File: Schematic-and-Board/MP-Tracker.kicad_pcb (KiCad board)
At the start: 2 copper layers, 61 parts, among them P1 DIL10, Q1 BC817, Q2 IRFR5303, Q3 BC817-40, Q4 IRFR5303, U1 MC34063, U2 TL082, U3 ATMEGA8-AI, U4 MC78L033, X1 3.6864MHz

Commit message: Update schematic and board design and firmware source.
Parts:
- removed D3, D6: 3V3, Diodes_SMD:SOD-123
- removed R17: 1k, Resistors_SMD:R_0805
- removed R18, R23, R24, R28, R29: 22k, Resistors_SMD:R_0805
- added ?: , Mounting_Holes:MountingHole_3.2mm_M3_DIN965, F.Cu at (167.6, 70.5)
- added ?: , Mounting_Holes:MountingHole_3.2mm_M3_DIN965, F.Cu at (99.9, 141.5)
- added C14: 330u, Capacitors_SMD:c_elec_10x10, F.Cu at (151.7, 132.0)
- added C16: 470n, Capacitors_SMD:C_1206_HandSoldering, F.Cu at (150.3, 77.4)
- added C17: 470n, Capacitors_SMD:C_1206_HandSoldering, F.Cu at (123.2, 95.3)
- added C18: 470n, Capacitors_SMD:C_1206_HandSoldering, F.Cu at (127.3, 90.3)
- added D7: 1N4001, Diodes_SMD:SOD-323, F.Cu at (99.3, 134.5)
- added D9: 1N4001, Diodes_SMD:SOD-323, F.Cu at (159.3, 132.6)
- added L2: 10u, Choke_SMD:Choke_SMD_12x12mm_h8mm, F.Cu at (144.3, 116.8)
- added P2: CON_2x1, Pin_Headers:Pin_Header_Straight_1x02, F.Cu at (145.3, 70.3)
- added R11: 22k, Resistors_SMD:R_0805, F.Cu at (144.9, 90.0)
- added R31: 1K, Resistors_SMD:R_0805, F.Cu at (121.2, 91.8)
- added R32: 1K, Resistors_SMD:R_0805, F.Cu at (125.2, 92.7)
- added REF**: , Mounting_Holes:MountingHole_3.2mm_M3_DIN965, F.Cu at (100.6, 70.1)
- added REF**: , Mounting_Holes:MountingHole_3.2mm_M3_DIN965, F.Cu at (167.6, 141.2)
- C1, C10, C2, C3, C7: value 100n -> 470n; footprint Capacitors_SMD:C_0805 -> Capacitors_SMD:C_1206
- C12: value 10n -> 470n; footprint Capacitors_SMD:C_0805 -> Capacitors_SMD:C_1206
- C8: value 1n5 -> 68p
- L1: value 22u -> 100u
- P1: value DIL10 -> (none)
- Q1: value BC817 -> BC817-40
- R1: value 180R -> 1k
- R12: value 3k9 -> 3k3
- R13: value 3K9 -> 10k
- R15: footprint Resistors_SMD:R_0805 -> Resistors_SMD:R_1206
- R19: value 3k9 -> 10k
- R20: value 47k -> 27k
- R21: value 4k4 -> 2k35
- R22: value 1M -> 47
- R25: value 2k2 -> 1K
- U2: value TL082 -> TL081
- U3: value ATMEGA8-AI -> ATMEGA8
- moved R25 30.5 mm to (124.4, 69.7)
- moved R10 19.0 mm to (134.9, 91.0), turned to 0 degrees
- moved R26 15.6 mm to (139.1, 76.5)
- moved R5 14.0 mm to (154.8, 103.6)
- moved D2 11.9 mm to (166.5, 132.6), turned to 270 degrees
- moved C9 11.7 mm to (101.7, 134.9)
- moved D1 11.4 mm to (104.0, 114.8), turned to 0 degrees
- moved C6 11.3 mm to (109.0, 131.4)
- moved R15 11.3 mm to (139.4, 93.9)
- moved R19 11.3 mm to (144.0, 86.1)
- moved R2 11.3 mm to (103.4, 109.5)
- moved R4 11.3 mm to (155.8, 111.6)
- moved R8 11.3 mm to (125.5, 75.9)
- moved C5 11.3 mm to (103.2, 94.0)
- moved C1 11.3 mm to (133.5, 86.0)
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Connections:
- D1 pad 1: Net-(D1-Pad1) -> Net-(D1-Pad2)
- D1 pad 2: Net-(D1-Pad2) -> Net-(D1-Pad1)
- D2 pad 1: GNDPWR -> VAA
- D2 pad 2: VAA -> GNDPWR
- P1 pad 10: +3.3V -> GNDPWR
- P1 pad 4: Net-(P1-Pad4) -> +3.3V
- P1 pad 7: GNDPWR -> Net-(P1-Pad7)
- R10 pad 1: Net-(R10-Pad1) -> Net-(C18-Pad1)
- R22 pad 1: Net-(R18-Pad2) -> VCC
- R22 pad 2: GNDPWR -> Net-(C16-Pad1)
- R25 pad 1: Net-(R18-Pad2) -> Net-(R25-Pad1)
- U2 pad 1: Net-(R19-Pad1) -> (no net)
- U2 pad 5: Net-(R23-Pad2) -> (no net)
- U2 pad 6: Net-(R18-Pad2) -> Net-(R19-Pad1)
- U2 pad 7: Net-(R17-Pad2) -> Net-(C16-Pad1)
- U2 pad 8: VCC -> (no net)
- U3 pad 1: Net-(U3-Pad1) -> (no net)
- U3 pad 10: Net-(U3-Pad10) -> (no net)
- U3 pad 12: Net-(U3-Pad12) -> (no net)
- U3 pad 13: Net-(R10-Pad1) -> Net-(R31-Pad1)
- U3 pad 14: Net-(U3-Pad14) -> (no net)
- U3 pad 16: Net-(P1-Pad5) -> Net-(P1-Pad2)
- U3 pad 17: Net-(P1-Pad4) -> Net-(P1-Pad3)
- U3 pad 19: Net-(U3-Pad19) -> (no net)
- U3 pad 2: Net-(U3-Pad2) -> (no net)
- U3 pad 22: Net-(U3-Pad22) -> (no net)
- U3 pad 24: Net-(D3-Pad1) -> (no net)
- U3 pad 26: Net-(U3-Pad26) -> Net-(R25-Pad1)
- U3 pad 27: Net-(U3-Pad27) -> (no net)
- U3 pad 28: Net-(U3-Pad28) -> (no net)
- U3 pad 29: Net-(P1-Pad3) -> Net-(P1-Pad9)
- U3 pad 30: Net-(P1-Pad9) -> Net-(P1-Pad7)
- U3 pad 31: Net-(P1-Pad2) -> Net-(P1-Pad5)
- U3 pad 32: Net-(U3-Pad32) -> (no net)
- U3 pad 9: Net-(U3-Pad9) -> (no net)
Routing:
- net GNDPWR: track 471.2 -> 756.0 mm, vias 16 -> 25
- net VCC: track 180.8 -> 282.0 mm
- net Net-(Q3-Pad1): track 169.8 -> 259.6 mm
- net Net-(P1-Pad2): track 13.5 -> 99.0 mm
- net Net-(P1-Pad4): track 84.9 -> 0.00 mm
- net Net-(P1-Pad5): track 74.4 -> 11.1 mm
- net Net-(P1-Pad1): track 54.3 -> 92.9 mm
- net +3.3V: track 59.7 -> 93.0 mm
- net +BATT: track 121.4 -> 147.9 mm
- net Net-(R19-Pad2): track 32.3 -> 51.6 mm
- net Net-(R17-Pad2): track 18.5 -> 0.00 mm
- net Net-(Q3-Pad3): track 42.3 -> 23.9 mm
- net Net-(P1-Pad3): track 19.6 -> 36.4 mm
- net Net-(C18-Pad1): track 0.00 -> 16.0 mm
- net Net-(R18-Pad2): track 15.7 -> 0.00 mm
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- added copper zone on B.Cu, net GNDPWR
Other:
- net class Small added: clearance 0.2, trace_width 0.2, via_dia 1, via_drill 0.8
- board text added: "3V3"
- board text added: "GND"
- board text added: "MISO"
- board text added: "MOSI"
- board text added: "RST"
- board text added: "RX"
- board text added: "SCL"
- board text added: "TX"

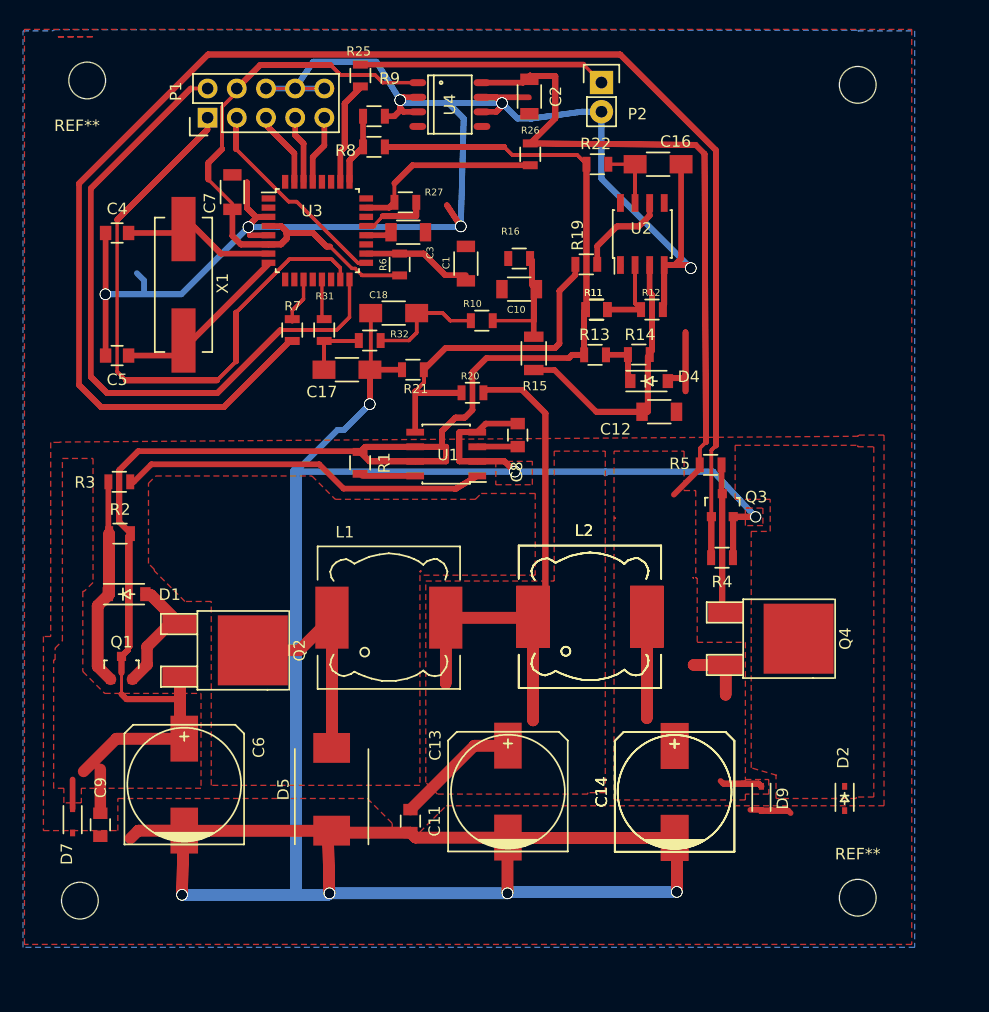
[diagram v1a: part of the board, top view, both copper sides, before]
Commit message: Updated firmware with temperature sensor support (KTY81-210) Minor fixes in the schematic.
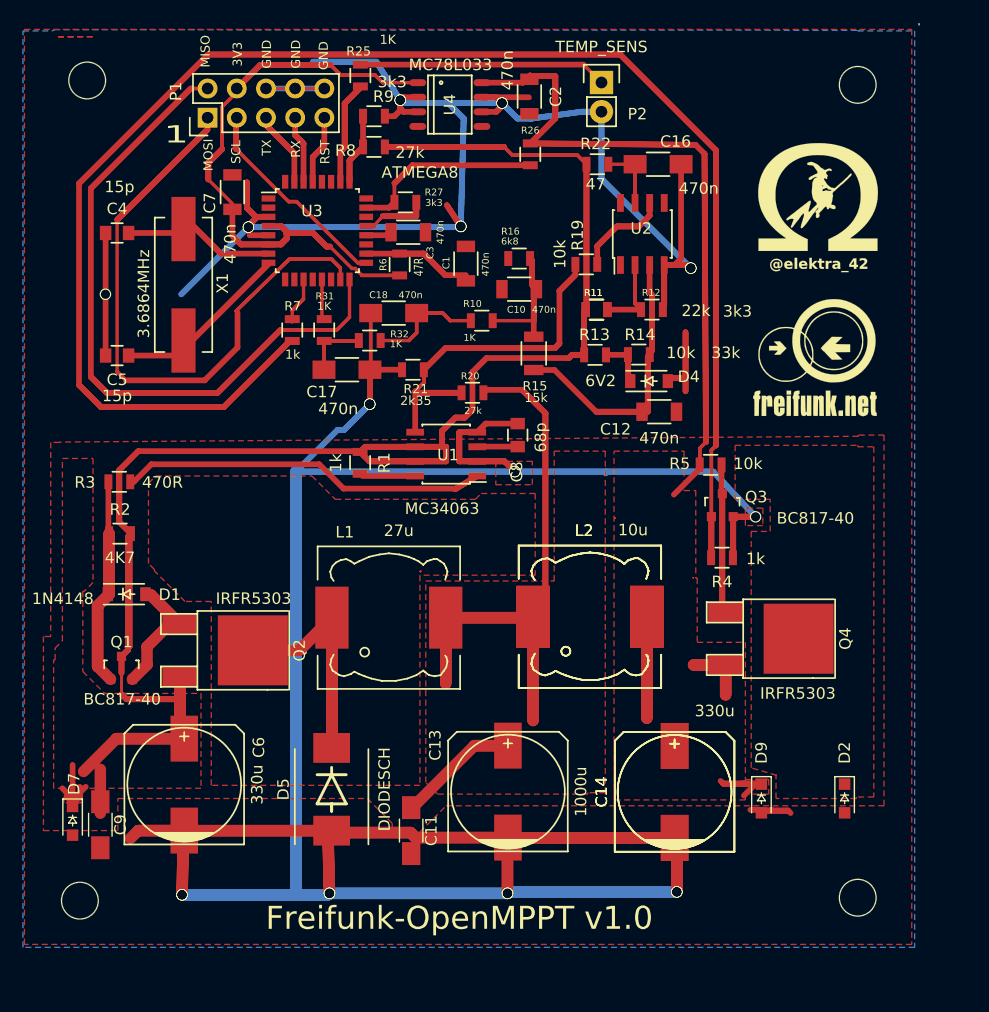
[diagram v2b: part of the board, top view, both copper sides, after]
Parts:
- added ?: , ELEKTRONIK:elektra-hexenlogo, F.Cu at (164.2, 81.2)
- added ?: , ELEKTRONIK:Freifunk-Logo, F.Cu at (164.0, 94.1)
- C11, C9: footprint Capacitors_SMD:C_0805 -> Capacitors_SMD:C_1206_HandSoldering
- C14: value 330u -> (none)
- D2, D7, D9: footprint Diodes_SMD:SOD-323 -> ELEKTRONIK:D_SOD-323_HandSoldering
- D5: footprint Diodes_SMD:DO-214AB -> ELEKTRONIK:DO-214AB
- L1: value 100u -> 27u
- L2: value 10u -> (none)
- P2: value CON_2x1 -> TEMP_SENS
- moved C11 0.83 mm to (128.8, 135.4)
- renumbered REF** to ?
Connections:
- D7 pad 1: GNDPWR -> VCC
- D7 pad 2: VCC -> GNDPWR
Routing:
- net GNDPWR: track 756.0 -> 737.2 mm, vias 25 -> 24
- net Net-(P1-Pad1): track 92.9 -> 77.6 mm
- net VCC: track 282.0 -> 289.0 mm
- net (no net): track 2.12 -> 0.08 mm
- net +BATT: track 147.9 -> 149.9 mm
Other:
- board text added: "1"
- board text added: "Freifunk-OpenMPPT v1.0"
